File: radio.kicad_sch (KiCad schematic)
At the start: 41 parts, among them J301 434MHz ANT pads, U301 CC1200, X301 40MHz

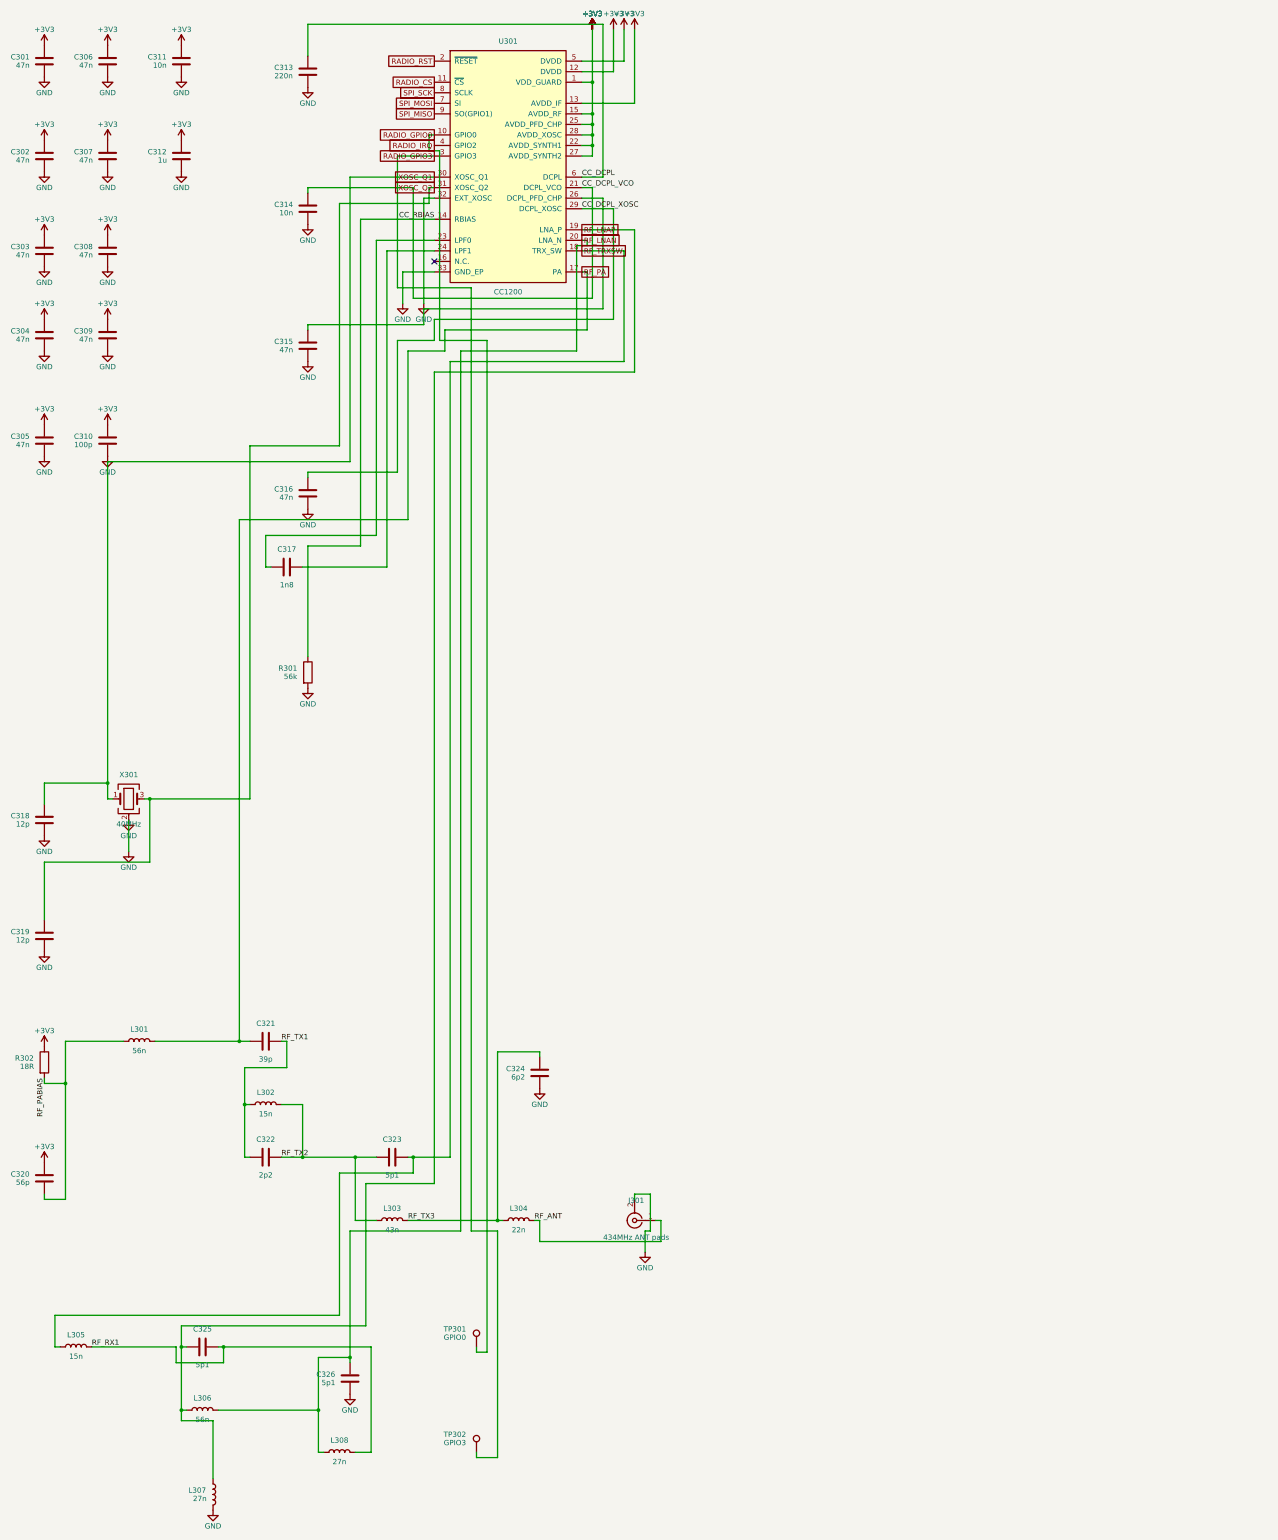
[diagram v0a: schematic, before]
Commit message: Remove the buck-boost: run straight off a 3.6 V max cell
The TPS63001 and its inductor come out and the battery drives the board
directly, so the rail is renamed +3V3 -> +BATT on every sheet: a net called
3V3 that is really the cell is the kind of label someone connects a charger
to.

SW101 used to switch the converter's EN pin, which is why it was never in
series with the load - the C&K JS series is rated 300 mA and this board
peaks past that. With no EN pin it now drives the gate of Q102, a second
DMG3401LSN-7 back to back with the reverse-block Q101. Q101 keeps its source
on the load side so its body diode conducts forward, which is exactly why it
cannot also be the switch; Q102 faces the other way so an open channel
really disconnects.

R102/C102 are re-used as a 10k/1u gate network giving about 9 ms of soft
start, replacing the converter's. Without it the switch would connect ~70 uF
of rail and IC decoupling straight across a cell that may have ohms of
internal resistance. The 10k stays small against the 100k pull-up so the
gate still reaches 91 % of VBATT.

The R103/R104 sense divider moves from VBATT to the switched +BATT, so it
draws nothing with the board off.

Also fixes assemble.ts rewriting cc1200_balloon.kicad_pro from a fixed
template every build, which was silently resetting the net classes, board
design settings and ERC severities KiCad had written. Found while rebuilding
for this change.

Gates: placement 5/5, routing DRC 0, netlist matches sheets/*.json at 378
endpoints / 76 nets, full-hierarchy ERC 0 errors and the 2 known BME688
address-strap warnings. Build output is byte-identical across runs.

The large .kicad_sch diffs are formatting: the committed set had been opened
and saved by KiCad, which expands the compact s-expressions the generator
writes. Nothing but the power sheet and the rail name changed electrically.

Not done: cc1200_balloon.kicad_pcb still carries U101, L101 and C105 and has
no Q102. It needs Update PCB from Schematic.

Co-Au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
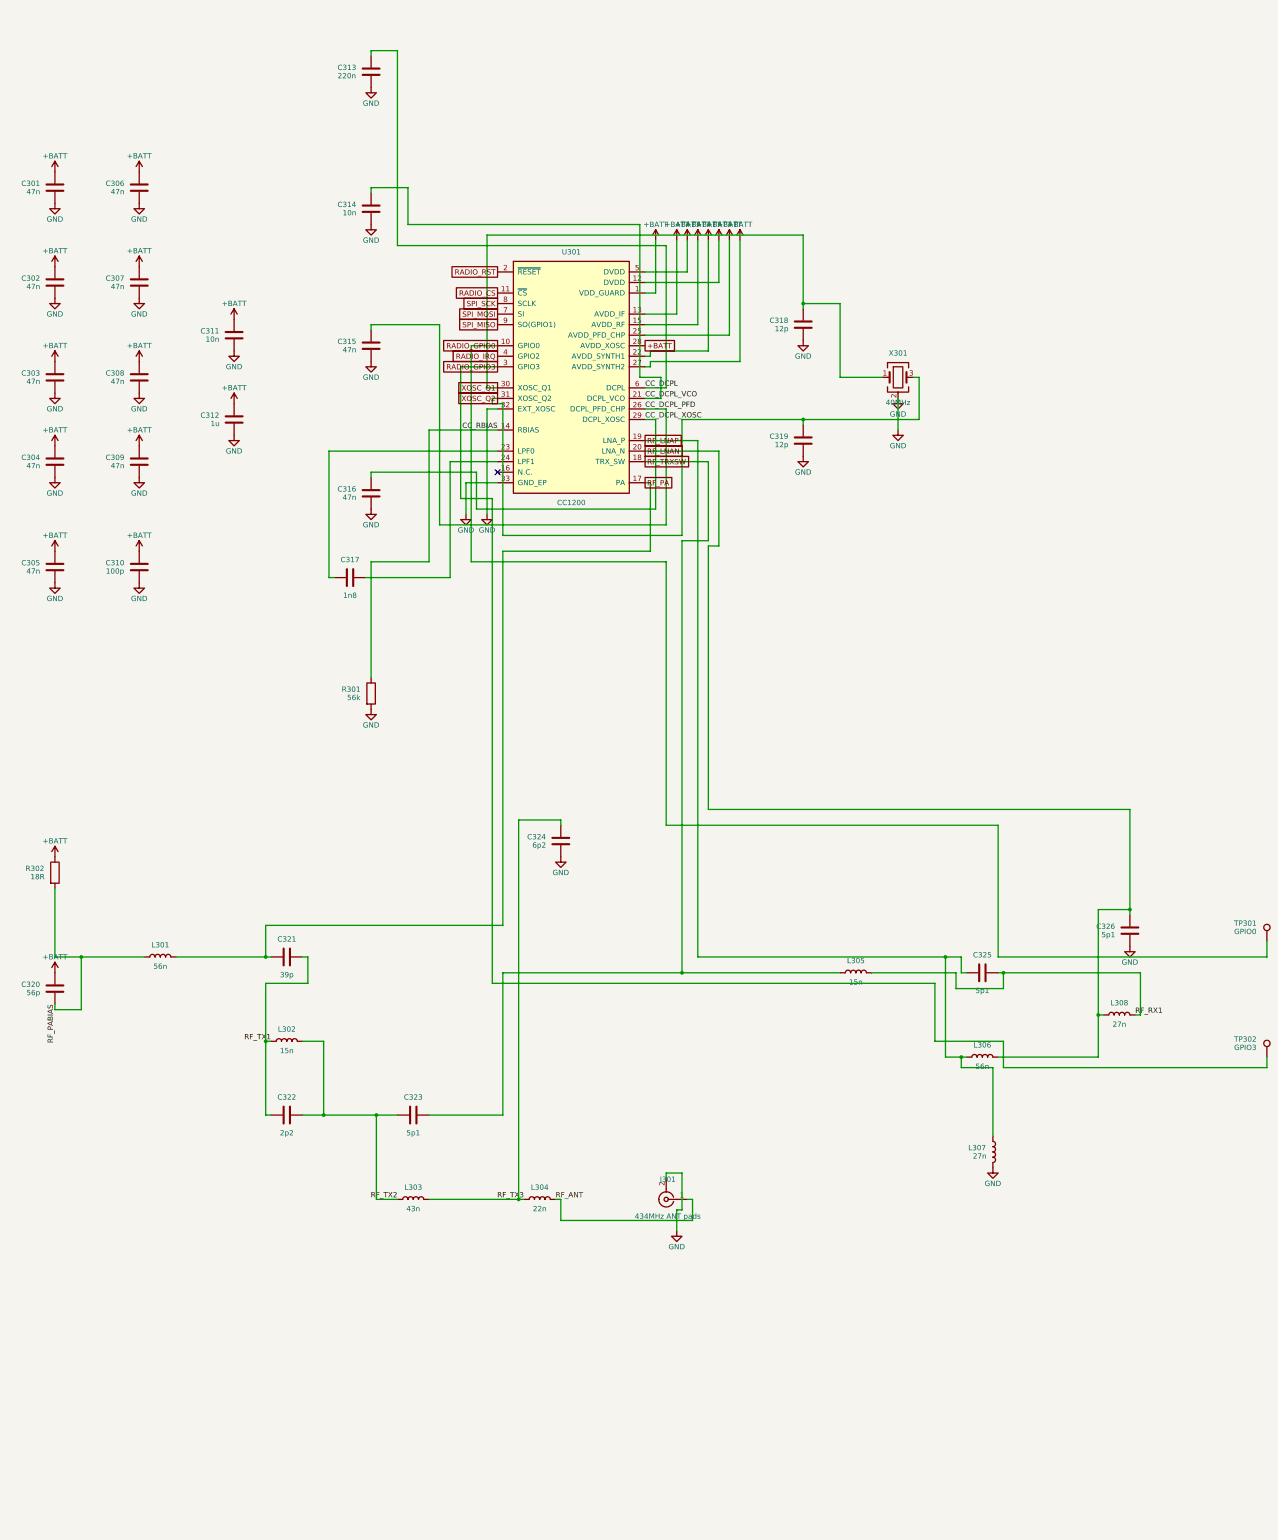
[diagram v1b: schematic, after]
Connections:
- net CC_DCPL_PFD: now reaches C315.1, U301.26 (DCPL_PFD_CHP)
- net +3V3 renamed +BATT
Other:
- moved on the sheet: C301, C302, C303, C304, C305, C306, C307, C308, C309, C310, C311, C312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
